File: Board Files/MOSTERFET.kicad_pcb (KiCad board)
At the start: 2 copper layers, 50 x 60 mm, 34 parts, among them CN11 Jumper_NC_Small, CN21 Jumper_NC_Small, J11 XT-60-M, J12 XT-60-F, J21 XT-60-M, J22 XT-60-F, Q11 AUIRFSA8409-7P, Q21 AUIRFSA8409-7P, U11 TLP182, U21 TLP182

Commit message: cleaned up baord files
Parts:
- moved REF*** 3.00 mm to (89.0, 112.0)
- moved LO1 2.30 mm to (103.0, 112.0)
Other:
- outline, holes or cut-outs redrawn
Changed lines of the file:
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@@
   (general
     (thickness 1.6)
-    (drawings 34)
+    (drawings 32)
     (tracks 205)
     (zones 0)
@@
   )
   (module Symbols:KiCad-Logo2_6mm_SilkScreen (layer F.Cu)
-    (at 92 112.1)
+    (at 89 112)
     (descr "KiCad Logo")
     (tags "Logo KiCad")
@@
   )
   (module Symbols:OSHW-Symbol_8.9x8mm_SilkScreen (layer F.Cu)
-    (at 105.3 111.9)
+    (at 103 112)
     (descr "Open Source Hardware Symbol")
     (tags "Logo Symbol OSHW")
@@
   (gr_line (start 73 113) (end 77 113) (layer Dwgs.User) (width 0.3))
   (gr_line (start 119 57) (end 119 61) (layer Dwgs.User) (width 0.3))
-  (target plus (at 73 117) (size 5) (width 0.15) (layer Edge.Cuts))
   (gr_text "MOSTER FET is licensed under a\nCreative Commons Attribution-ShareAlike \n3.0 Unported License." (at 85.25 66.5 90) (layer B.Cu)
     (effects (font (size 1.5 1.5) (thickness 0.3)) (justify left mirror))
@@
     (effects (font (size 1 1) (thickness 0.1)) (justify left))
   )
-  (gr_line (start 73 117) (end 73.25 117) (angle 90) (layer Edge.Cuts) (width 0.15))
   (via (at 100.65 102.3) (size 0.6) (drill 0.4) (layers F.Cu B.Cu) (net 1))
   (via (at 98.15 103.2) (size 0.6) (drill 0.4) (layers F.Cu B.Cu) (net 1))

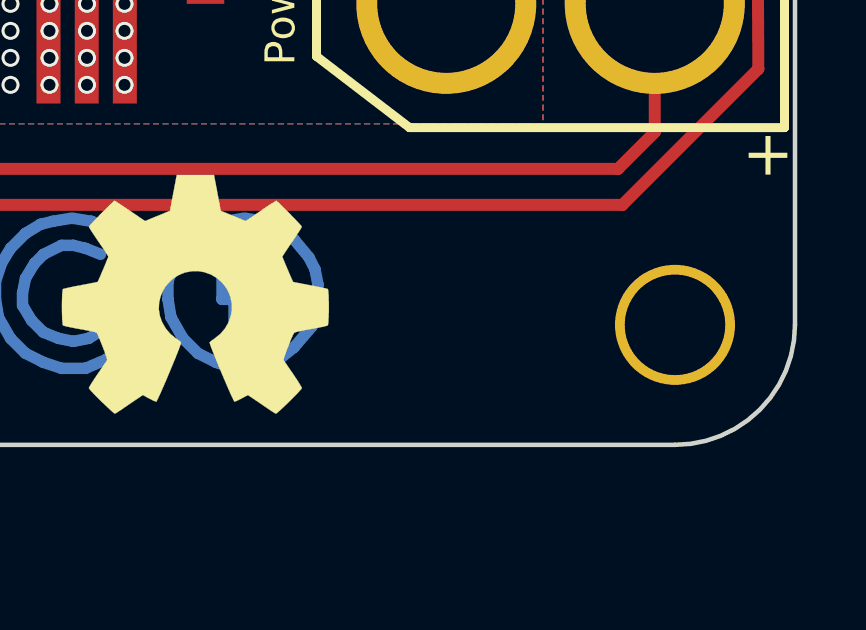
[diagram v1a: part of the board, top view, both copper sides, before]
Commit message: Added OSHWA number to board and documents
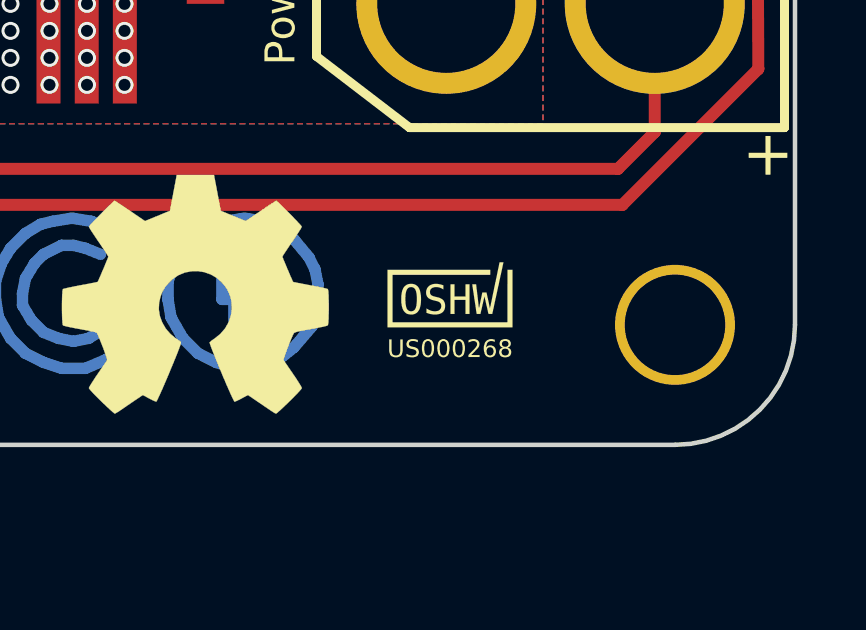
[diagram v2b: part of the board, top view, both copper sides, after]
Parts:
- added OSHW_Mono_0.1_Scale: US000268, kicad-oshwa:OSHW_Mono_0.1_Scale, F.Cu at (111.5, 112.0)
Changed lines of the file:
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@@
     (tracks 205)
     (zones 0)
-    (modules 34)
+    (modules 35)
     (nets 17)
   )
@@
     (uvia_drill 0.1)
   )
+  (module kicad-oshwa:OSHW_Mono_0.1_Scale (layer F.Cu)
+    (at 111.5 112)
+    (fp_text reference OSHW_Mono_0.1_Scale (at 0 -4.132151) (layer F.SilkS) hide
+      (effects (font (size 1.524 1.524) (thickness 0.3048)))
+    )
+    (fp_text value US000268 (at 0 1.8) (layer F.SilkS)
+      (effects (font (size 0.59 0.59) (thickness 0.08)))
+    )
+    (fp_poly (pts (xy 0.740946 -0.350373) (xy 0.871253 -0.350373) (xy 0.965841 0.451314) (xy 1.078289 -0.079175)
+      (xy 1.217857 -0.079175) (xy 1.331628 0.452637) (xy 1.651994 -1.084151) (xy 1.782302 -1.084151)
+      (xy 1.409018 0.637184) (xy 1.28268 0.637184) (xy 1.148404 0.050471) (xy 1.014789 0.637184)
+      (xy 0.888451 0.637184) (xy 0.740946 -0.350373)) (layer F.SilkS) (width 0.00254))
+    (fp_poly (pts (xy 0.016649 -0.350373) (xy 0.150925 -0.350373) (xy 0.150925 0.054439) (xy 0.516711 0.054439)
+      (xy 0.516711 -0.350373) (xy 0.650987 -0.350373) (xy 0.650987 0.637184) (xy 0.516711 0.637184)
+      (xy 0.516711 0.166887) (xy 0.150925 0.166887) (xy 0.150925 0.637184) (xy 0.016649 0.637184)
+      (xy 0.016649 -0.350373)) (layer F.SilkS) (width 0.00254))
+    (fp_poly (pts (xy -0.219492 -0.316639) (xy -0.219492 -0.18104) (xy -0.260135 -0.204925) (xy -0.300925 -0.224549)
+      (xy -0.341862 -0.23991) (xy -0.382578 -0.250933) (xy -0.423589 -0.257548) (xy -0.464893 -0.259754)
+      (xy -0.523542 -0.254829) (xy -0.573372 -0.240056) (xy -0.614383 -0.215436) (xy -0.644883 -0.182877)
+      (xy -0.663184 -0.14341) (xy -0.669284 -0.097035) (xy -0.660354 -0.039322) (xy -0.633565 0.002846)
+      (xy -0.602403 0.024527) (xy -0.557424 0.043709) (xy -0.498627 0.060392) (xy -0.428513 0.076267)
+      (xy -0.375967 0.090714) (xy -0.329453 0.108123) (xy -0.288972 0.128496) (xy -0.254523 0.151832)
+      (xy -0.226106 0.178132) (xy -0.198326 0.216001) (xy -0.178482 0.260153) (xy -0.166576 0.310589)
+      (xy -0.162606 0.367309) (xy -0.166099 0.420993) (xy -0.176577 0.469332) (xy -0.194039 0.512327)
+      (xy -0.218487 0.549977) (xy -0.249919 0.582283) (xy -0.288019 0.608953) (xy -0.332469 0.629696)
+      (xy -0.383269 0.644513) (xy -0.440419 0.653403) (xy -0.503919 0.656366) (xy -0.550295 0.654676)
+      (xy -0.596817 0.649605) (xy -0.643487 0.641153) (xy -0.690303 0.629761) (xy -0.737267 0.614988)
+      (xy -0.784377 0.596835) (xy -0.784377 0.454621) (xy -0.734621 0.483946) (xy -0.686776 0.507538)
+      (xy -0.640841 0.525397) (xy -0.595347 0.537892) (xy -0.549707 0.545388) (xy -0.503919 0.547887)
+      (xy -0.456129 0.545076) (xy -0.413961 0.536642) (xy -0.377415 0.522586) (xy -0.346492 0.502908)
+      (xy -0.315257 0.468512) (xy -0.296515 0.426179) (xy -0.290268 0.375908) (xy -0.294604 0.330415)
+      (xy -0.307613 0.292711) (xy -0.329294 0.262798) (xy -0.361265 0.238766) (xy -0.406023 0.218702)
+      (xy -0.46357 0.202606) (xy -0.535008 0.186069) (xy -0.587025 0.172364) (xy -0.633009 0.156119)
+      (xy -0.672961 0.137333) (xy -0.706881 0.116008) (xy -0.734768 0.092142) (xy -0.76197 0.058036)
+      (xy -0.781401 0.018556) (xy -0.793059 -0.0263) (xy -0.796945 -0.076529) (xy -0.7934 -0.127329)
+      (xy -0.782763 -0.173896) (xy -0.765036 -0.216229) (xy -0.740218 -0.254329) (xy -0.708309 -0.288196)
+      (xy -0.670263 -0.317009) (xy -0.627559 -0.339419) (xy -0.580199 -0.355426) (xy -0.528181 -0.365031)
+      (xy -0.471508 -0.368233) (xy -0.432923 -0.366762) (xy -0.393015 -0.362352) (xy -0.351784 -0.355004)
+      (xy -0.309157 -0.345155) (xy -0.265059 -0.332366) (xy -0.219492 -0.316639)) (layer F.SilkS) (width 0.00254))
+    (fp_poly (pts (xy -1.105184 0.144397) (xy -0.965617 0.144397) (xy -0.966899 0.206843) (xy -0.970744 0.265196)
+      (xy -0.977152 0.319457) (xy -0.986123 0.369624) (xy -0.997657 0.415699) (xy -1.011754 0.457681)
+      (xy -1.028414 0.49557) (xy -1.047638 0.529366) (xy -1.077146 0.568172) (xy -1.111432 0.599922)
+      (xy -1.150495 0.624616) (xy -1.194335 0.642255) (xy -1.242952 0.652839) (xy -1.296346 0.656366)
+      (xy -1.349741 0.652857) (xy -1.398358 0.642329) (xy -1.442198 0.624782) (xy -1.481261 0.600216)
+      (xy -1.515546 0.568631) (xy -1.545054 0.530028) (xy -1.564123 0.496366) (xy -1.580649 0.458549)
+      (xy -1.594633 0.416577) (xy -1.606074 0.370451) (xy -1.614973 0.32017) (xy -1.621329 0.265734)
+      (xy -1.625142 0.207143) (xy -1.626414 0.144397) (xy -1.625142 0.081797) (xy -1.621329 0.02331)
+      (xy -1.614973 -0.031064) (xy -1.606074 -0.081325) (xy -1.594633 -0.127472) (xy -1.580649 -0.169505)
+      (xy -1.564123 -0.207426) (xy -1.545054 -0.241233) (xy -1.515362 -0.280038) (xy -1.480967 -0.311788)
+      (xy -1.441867 -0.336482) (xy -1.398064 -0.354121) (xy -1.349557 -0.364704) (xy -1.296346 -0.368233)
+      (xy -1.242952 -0.364704) (xy -1.194335 -0.354121) (xy -1.150495 -0.336482) (xy -1.111432 -0.311788)
+      (xy -1.077146 -0.280038) (xy -1.047638 -0.241233) (xy -1.028414 -0.207426) (xy -1.011754 -0.169505)
+      (xy -0.997657 -0.127472) (xy -0.986123 -0.081325) (xy -0.977152 -0.031064) (xy -0.970744 0.02331)
+      (xy -0.966899 0.081797) (xy -0.965617 0.144397) (xy -1.105184 0.144397) (xy -1.106434 0.075312)
+      (xy -1.110183 0.013135) (xy -1.11643 -0.042133) (xy -1.125176 -0.090493) (xy -1.13642 -0.131945)
+      (xy -1.150164 -0.166488) (xy -1.17592 -0.207291) (xy -1.208869 -0.236436) (xy -1.249011 -0.253924)
+      (xy -1.296346 -0.259754) (xy -1.343434 -0.253924) (xy -1.383493 -0.236436) (xy -1.416525 -0.207291)
+      (xy -1.442528 -0.166488) (xy -1.45607 -0.131945) (xy -1.467149 -0.090493) (xy -1.475767 -0.042133)
+      (xy -1.481922 0.013135) (xy -1.485615 0.075312) (xy -1.486846 0.144397) (xy -1.485615 0.213281)
+      (xy -1.481922 0.275293) (xy -1.475767 0.330433) (xy -1.467149 0.378701) (xy -1.45607 0.420097)
+      (xy -1.442528 0.454621) (xy -1.416525 0.495425) (xy -1.383493 0.524571) (xy -1.343434 0.542058)
+      (xy -1.296346 0.547887) (xy -1.249011 0.542099) (xy -1.208869 0.524736) (xy -1.17592 0.495797)
+      (xy -1.150164 0.455283) (xy -1.13642 0.42074) (xy -1.125176 0.379289) (xy -1.11643 0.330929)
+      (xy -1.110183 0.27566) (xy -1.106434 0.213483) (xy -1.105184 0.144397)) (layer F.SilkS) (width 0.00254))
+    (fp_poly (pts (xy -2.082271 -0.836724) (xy -2.082271 -0.752057) (xy -2.082271 0.999484) (xy -2.082271 1.084151)
+      (xy -1.997604 1.084151) (xy 1.997604 1.084151) (xy 2.082271 1.084151) (xy 2.082271 0.999484)
+      (xy 2.082271 -0.836724) (xy 1.916572 -0.836724) (xy 1.912938 0.914818) (xy -1.912938 0.914818)
+      (xy -1.912938 -0.667391) (xy 1.342319 -0.667391) (xy 1.342319 -0.836724) (xy -1.997604 -0.836724)
+      (xy -2.082271 -0.836724)) (layer F.SilkS) (width 0.00254))
+  )
   (module Symbols:Symbol_CreativeCommons_CopperTop_Type2_Small (layer B.Cu)

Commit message: LED not on placment diagrams
LED Value was ~ needed to be a part number so they showed up in the graphical bom
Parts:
- D13, D23: value ~ -> QBLP631-IW
- renumbered OSHW_Mono_0.1_Scale to OSHW
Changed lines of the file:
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@@
   (module kicad-oshwa:OSHW_Mono_0.1_Scale (layer F.Cu)
     (at 111.5 112)
-    (fp_text reference OSHW_Mono_0.1_Scale (at 0 -4.132151) (layer F.SilkS) hide
+    (fp_text reference OSHW (at 0 -4.132151) (layer F.SilkS) hide
       (effects (font (size 1.524 1.524) (thickness 0.3048)))
     )
@@
       (effects (font (size 1 1) (thickness 0.15)))
     )
-    (fp_text value ~ (at 0 1.75 270) (layer F.Fab)
+    (fp_text value QBLP631-IW (at 0 1.75 270) (layer F.Fab)
       (effects (font (size 1 1) (thickness 0.15)))
     )
@@
       (effects (font (size 1 1) (thickness 0.15)))
     )
-    (fp_text value ~ (at 0 1.75 270) (layer F.Fab)
-      (effects (font (size 1 1) (thickness 0.15)))
-    )
+    (fp_text value QBLP631-IW (at 0 1.75 270) (layer F.Fab)
+      (effects (font (size 1 1) (thickness 0.15)))
+    )

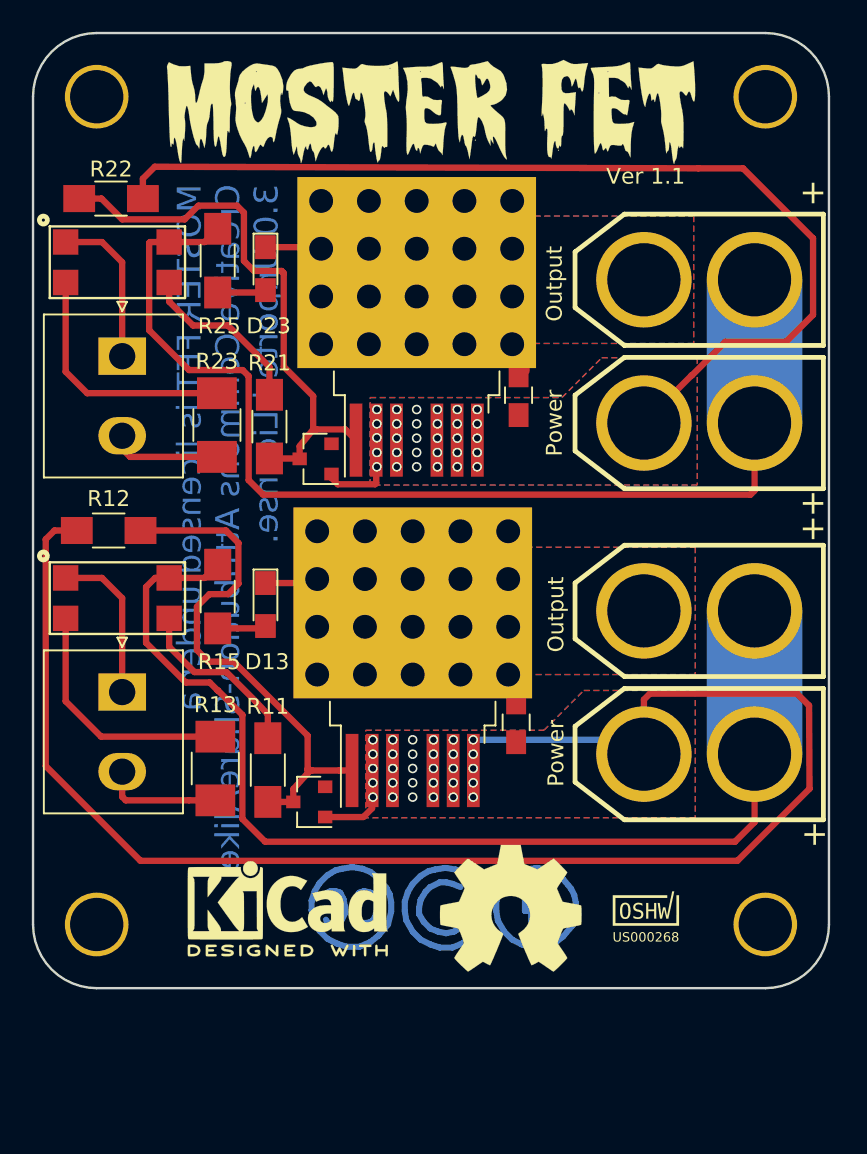
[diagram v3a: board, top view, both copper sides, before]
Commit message: Moved components for better diode soldering
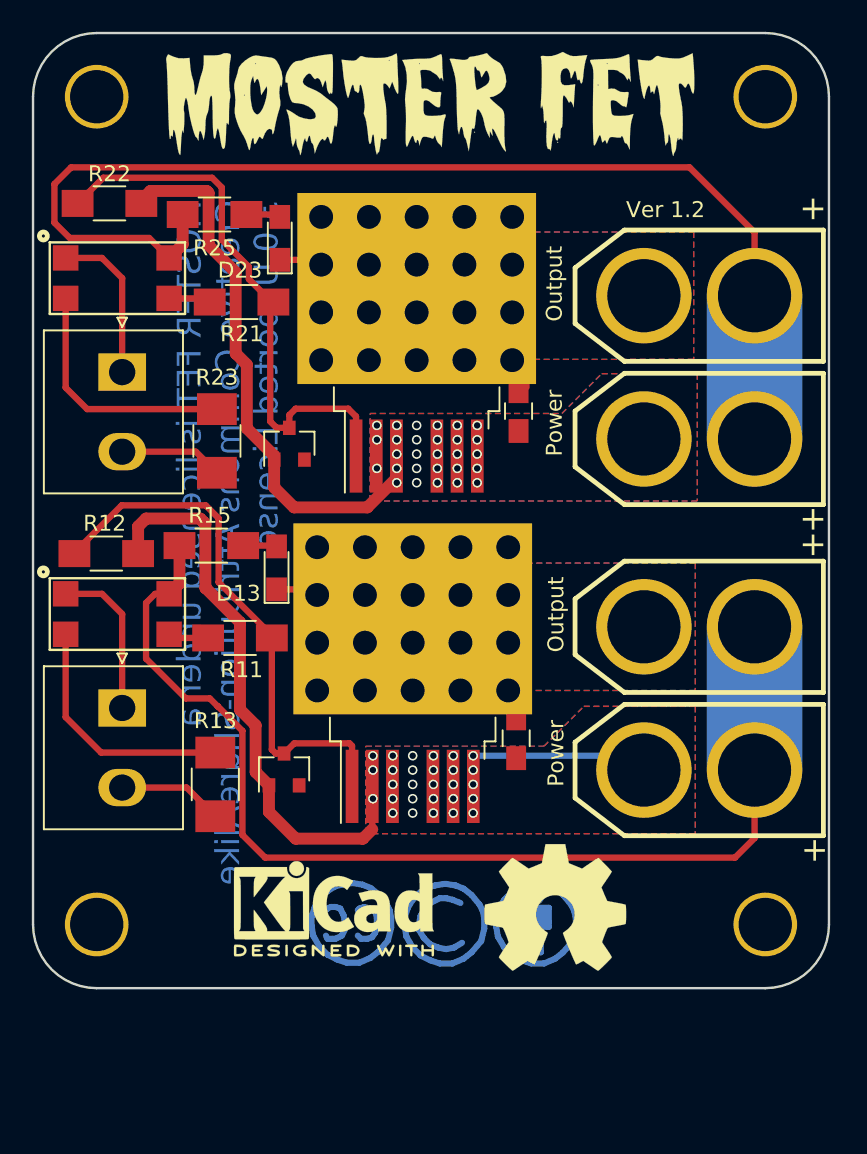
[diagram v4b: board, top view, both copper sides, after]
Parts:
- removed OSHW: US000268, kicad-oshwa:OSHW_Mono_0.1_Scale
- moved R11 8.48 mm to (86.0, 95.0), turned to 0 degrees
- moved R21 8.02 mm to (86.1, 73.9), turned to 0 degrees
- moved R15 3.22 mm to (84.2, 89.2), turned to 0 degrees
- moved R25 2.91 mm to (84.4, 68.4), turned to 0 degrees
- moved REF*** 2.90 mm to (91.9, 112.0)
- moved LO1 2.80 mm to (105.8, 112.0)
- moved D11 2.58 mm to (88.8, 103.3), turned to 90 degrees
- moved D13 2.40 mm to (88.3, 90.6), turned to 90 degrees
- moved D23 2.10 mm to (88.5, 69.9), turned to 90 degrees
- moved D21 1.90 mm to (89.1, 82.8), turned to 90 degrees
- moved R12 1.46 mm to (77.6, 89.7), turned to 0 degrees
- moved C11 1.00 mm to (103.3, 101.3)
- moved C21 1.00 mm to (103.5, 80.8)
- moved CN11 1.00 mm to (78.6, 99.4)
- moved CN21 1.00 mm to (78.6, 78.3)
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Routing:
- net GND: track 173.3 -> 81.3 mm, vias 60 -> 56
- net Net-(R11-Pad1): track 11.3 -> 2.55 mm
- net Net-(R21-Pad1): track 11.0 -> 2.65 mm
- net +BATT: track 139.9 -> 142.2 mm
- net Net-(D11-Pad3): track 33.1 -> 34.6 mm
- net Net-(D13-Pad2): track 3.06 -> 2.12 mm
- net Net-(CN11-Pad2): track 7.52 -> 6.60 mm
- net Net-(D23-Pad2): track 3.06 -> 2.16 mm
- net Net-(C21-Pad1): track 7.00 -> 6.32 mm
- net Net-(C11-Pad1): track 5.31 -> 4.65 mm
- net Net-(D21-Pad3): track 34.9 -> 35.4 mm
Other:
- board text added: "Ver 1.2"
- board text removed: "Ver 1.1"
